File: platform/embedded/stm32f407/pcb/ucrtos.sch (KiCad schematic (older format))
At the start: 7 parts, among them J1 nes_gamepad, J2 STM32F4_Discovery_Header

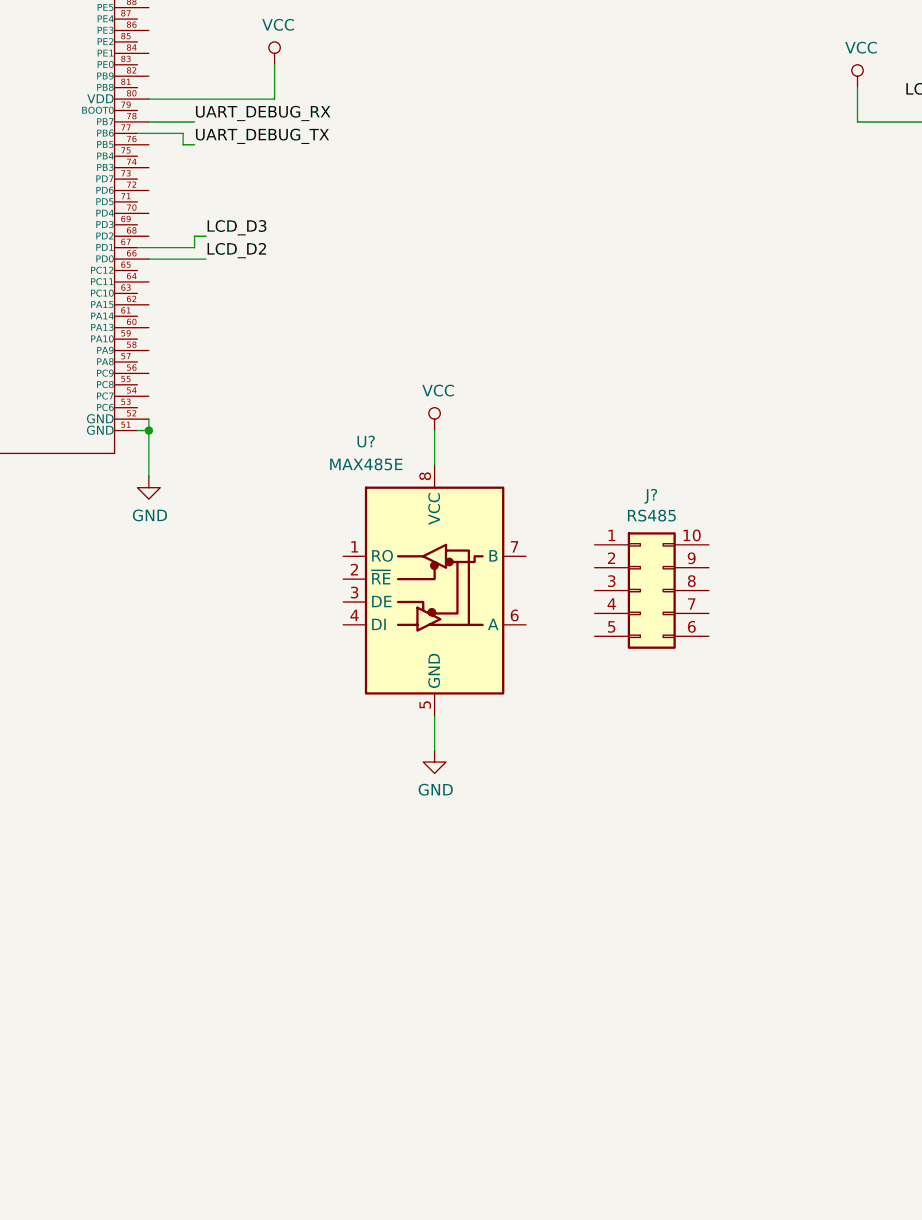
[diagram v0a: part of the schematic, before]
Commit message: platform stm32f4: pcb: add NRF24
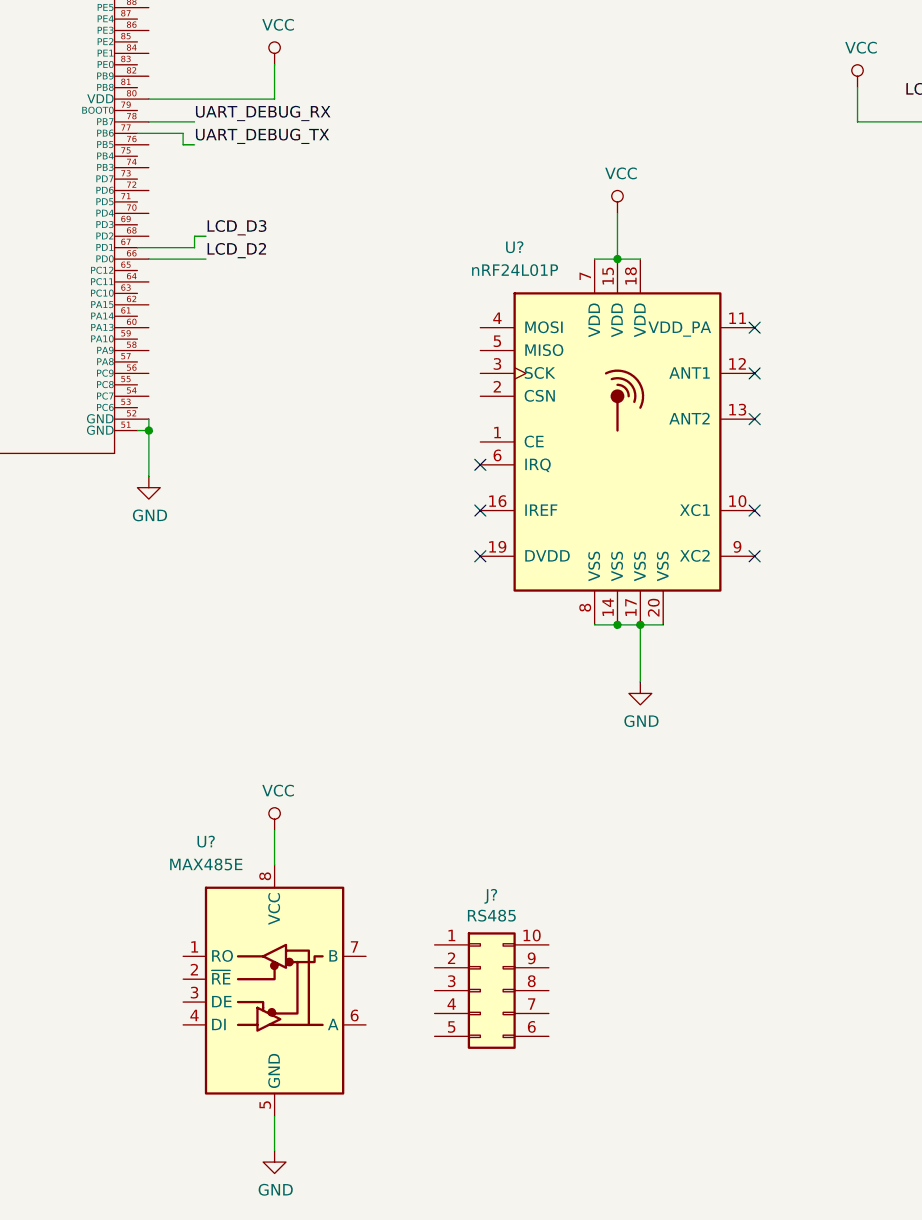
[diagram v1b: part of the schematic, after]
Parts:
- added U?: nRF24L01P, Package_DFN_QFN:QFN-20-1EP_4x4mm_P0.5mm_EP2.5x2.5mm, symbol RF:nRF24L01P
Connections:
- net GND: now also U?.14 (VSS), U?.17 (VSS), U?.20 (VSS), U?.8 (VSS)
- net VCC: now also U?.15 (VDD), U?.18 (VDD), U?.7 (VDD)
- no-connect marks 13 -> 21
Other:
- moved on the sheet: J?, U?
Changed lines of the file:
@@
 L Interface_UART:MAX485E U?
 U 1 1 5C438854
-P 6150 4450
-F 0 "U?" H 5850 5050 50  0000 C CNN
-F 1 "MAX485E" H 5850 4950 50  0000 C CNN
-F 2 "" H 6150 3750 50  0001 C CNN
-F 3 "https://datasheets.maximintegrated.com/en/ds/MAX1487E-MAX491E.pdf" H 6150 4500 50  0001 C CNN
-	1    6150 4450
+P 5450 6200
+F 0 "U?" H 5150 6800 50  0000 C CNN
+F 1 "MAX485E" H 5150 6700 50  0000 C CNN
+F 2 "" H 5450 5500 50  0001 C CNN
+F 3 "https://datasheets.maximintegrated.com/en/ds/MAX1487E-MAX491E.pdf" H 5450 6250 50  0001 C CNN
+	1    5450 6200
 	1    0    0    -1
 $EndComp
@@
 L Connector_Generic:Conn_02x05_Counter_Clockwise J?
 U 1 1 5C438977
-P 7050 4500
-F 0 "J?" H 7100 4917 50  0000 C CNN
-F 1 "RS485" H 7100 4826 50  0000 C CNN
-F 2 "" H 7050 4500 50  0001 C CNN
-F 3 "~" H 7050 4500 50  0001 C CNN
-	1    7050 4500
+P 6350 6250
+F 0 "J?" H 6400 6667 50  0000 C CNN
+F 1 "RS485" H 6400 6576 50  0000 C CNN
+F 2 "" H 6350 6250 50  0001 C CNN
+F 3 "~" H 6350 6250 50  0001 C CNN
+	1    6350 6250
 	1    0    0    -1
 $EndComp
@@
 L power:VCC #PWR?
 U 1 1 5C4EA333
-P 6150 3800
-F 0 "#PWR?" H 6150 3650 50  0001 C CNN
-F 1 "VCC" H 6167 3973 50  0000 C CNN
-F 2 "" H 6150 3800 50  0001 C CNN
-F 3 "" H 6150 3800 50  0001 C CNN
-	1    6150 3800
-	1    0    0    -1
-$EndComp
-Wire Wire Line
-	6150 3800 6150 3950
+P 5450 5550
+F 0 "#PWR?" H 5450 5400 50  0001 C CNN
+F 1 "VCC" H 5467 5723 50  0000 C CNN
+F 2 "" H 5450 5550 50  0001 C CNN
+F 3 "" H 5450 5550 50  0001 C CNN
+	1    5450 5550
+	1    0    0    -1
+$EndComp
+Wire Wire Line
+	5450 5550 5450 5700
 $Comp
 L power:GND #PWR?
 U 1 1 5C4EB213
-P 6150 5200
-F 0 "#PWR?" H 6150 4950 50  0001 C CNN
-F 1 "GND" H 6155 5027 50  0000 C CNN
-F 2 "" H 6150 5200 50  0001 C CNN
-F 3 "" H 6150 5200 50  0001 C CNN
-	1    6150 5200
-	1    0    0    -1
-$EndComp
-Wire Wire Line
-	6150 5050 6150 5200
+P 5450 6950
+F 0 "#PWR?" H 5450 6700 50  0001 C CNN
+F 1 "GND" H 5455 6777 50  0000 C CNN
+F 2 "" H 5450 6950 50  0001 C CNN
+F 3 "" H 5450 6950 50  0001 C CNN
+	1    5450 6950
+	1    0    0    -1
+$EndComp
+Wire Wire Line
+	5450 6800 5450 6950
 $Comp
 L power:VCC #PWR?
@@
 Text Label 5100 2450 0    50   ~ 0
 UART_DEBUG_RX
+$Comp
+L RF:nRF24L01P U?
+U 1 1 5C63E83C
+P 6950 3850
+F 0 "U?" H 6500 4700 50  0000 C CNN
+F 1 "nRF24L01P" H 6500 4600 50  0000 C CNN
+F 2 "Package_DFN_QFN:QFN-20-1EP_4x4mm_P0.5mm_EP2.5x2.5mm" H 7150 4650 50  0001 L CIN
+F 3 "http://www.nordicsemi.com/eng/content/download/2726/34069/file/nRF24L01P_Product_Specification_1_0.pdf" H 6950 3950 50  0001 C CNN
+	1    6950 3850
+	1    0    0    -1
+$EndComp
+NoConn ~ 7550 3550
+NoConn ~ 7550 3750
+NoConn ~ 7550 4150
+NoConn ~ 7550 4350
+$Comp
+L power:GND #PWR?
+U 1 1 5C657D22
+P 7050 4900
+F 0 "#PWR?" H 7050 4650 50  0001 C CNN
+F 1 "GND" H 7055 4727 50  0000 C CNN
+F 2 "" H 7050 4900 50  0001 C CNN
+F 3 "" H 7050 4900 50  0001 C CNN
+	1    7050 4900
+	1    0    0    -1
+$EndComp
+Wire Wire Line
+	6850 4650 6950 4650
+Connection ~ 6950 4650
+Wire Wire Line
+	6950 4650 7050 4650
+Connection ~ 7050 4650
+Wire Wire Line
+	7050 4650 7150 4650
+$Comp
+L power:VCC #PWR?
+U 1 1 5C662322
+P 6950 2850
+F 0 "#PWR?" H 6950 2700 50  0001 C CNN
+F 1 "VCC" H 6967 3023 50  0000 C CNN
+F 2 "" H 6950 2850 50  0001 C CNN
+F 3 "" H 6950 2850 50  0001 C CNN
+	1    6950 2850
+	1    0    0    -1
+$EndComp
+Wire Wire Line
+	6850 3050 6950 3050
+Connection ~ 6950 3050
+Wire Wire Line
+	6950 3050 7050 3050
+Wire Wire Line
+	6950 3050 6950 2850
+Wire Wire Line
+	7050 4650 7050 4900
+NoConn ~ 6350 3950
+NoConn ~ 6350 4150
+NoConn ~ 6350 4350
+NoConn ~ 7550 3350
 $EndSCHEMATC

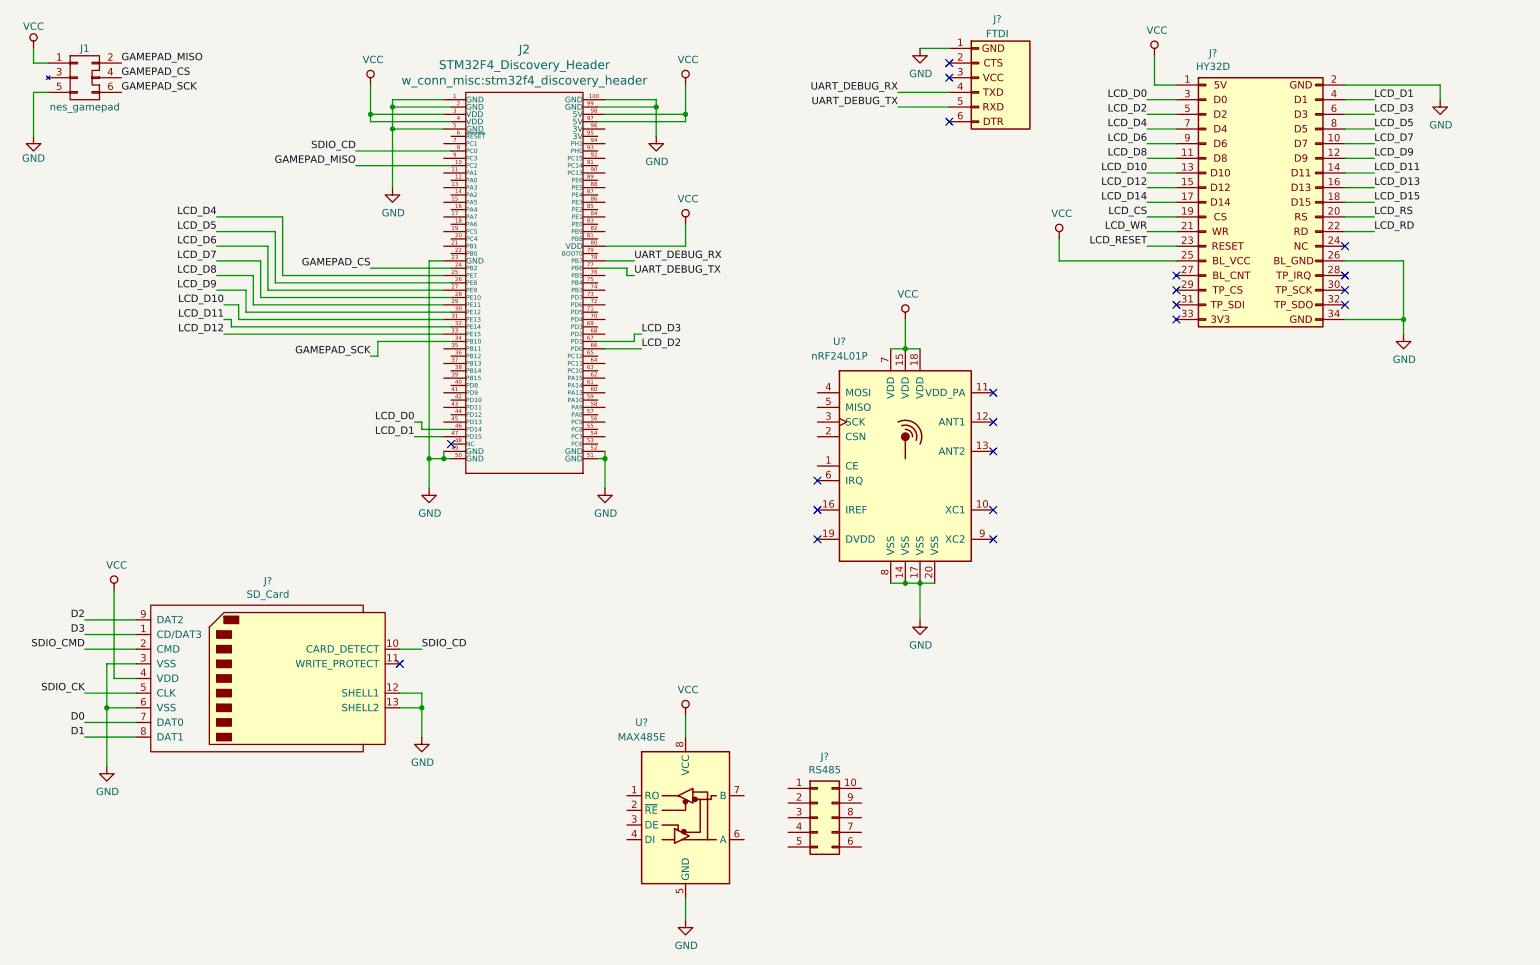
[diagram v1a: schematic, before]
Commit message: platform stm32f4: pcb: wire NRF24
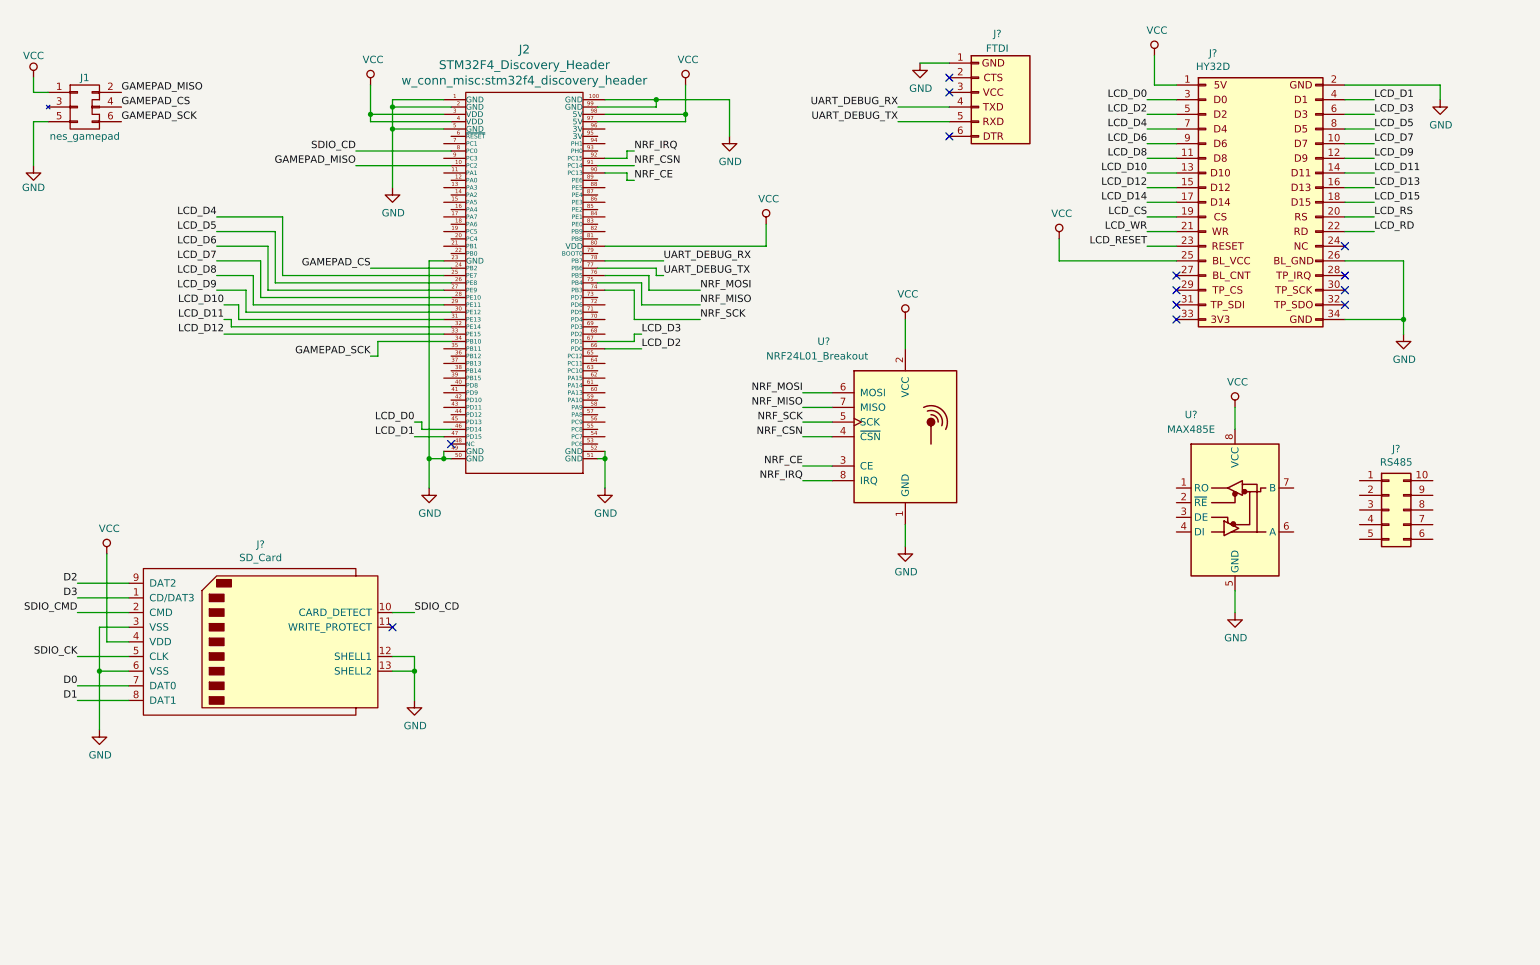
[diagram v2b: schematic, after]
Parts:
- removed U?: nRF24L01P, Package_DFN_QFN:QFN-20-1EP_4x4mm_P0.5mm_EP2.5x2.5mm, symbol RF:nRF24L01P
- added U?: NRF24L01_Breakout, RF_Module:nRF24L01_Breakout, symbol RF:NRF24L01_Breakout
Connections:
- net GND: now also U?.1 (GND)
- net VCC: now also U?.2 (VCC)
- net NRF_SCK: now reaches J2.74 (PB3)
- net NRF_SCK: now also U?.5 (SCK)
- net NRF_MISO: now reaches J2.75 (PB4)
- net NRF_MISO: now also U?.7 (MISO)
- net NRF_MOSI: now reaches J2.76 (PB5)
- net NRF_MOSI: now also U?.6 (MOSI)
- net NRF_CE: now reaches J2.90 (PC13)
- net NRF_CE: now also U?.3 (CE)
- net NRF_CSN: now reaches J2.91 (PC14)
- net NRF_CSN: now also U?.4 (~CSN)
- net NRF_IRQ: now reaches J2.92 (PC15)
- net NRF_IRQ: now also U?.8 (IRQ)
- no-connect marks 21 -> 13
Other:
- moved on the sheet: J1, J?, U?

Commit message: platform stm32f4: pcb: update schematics
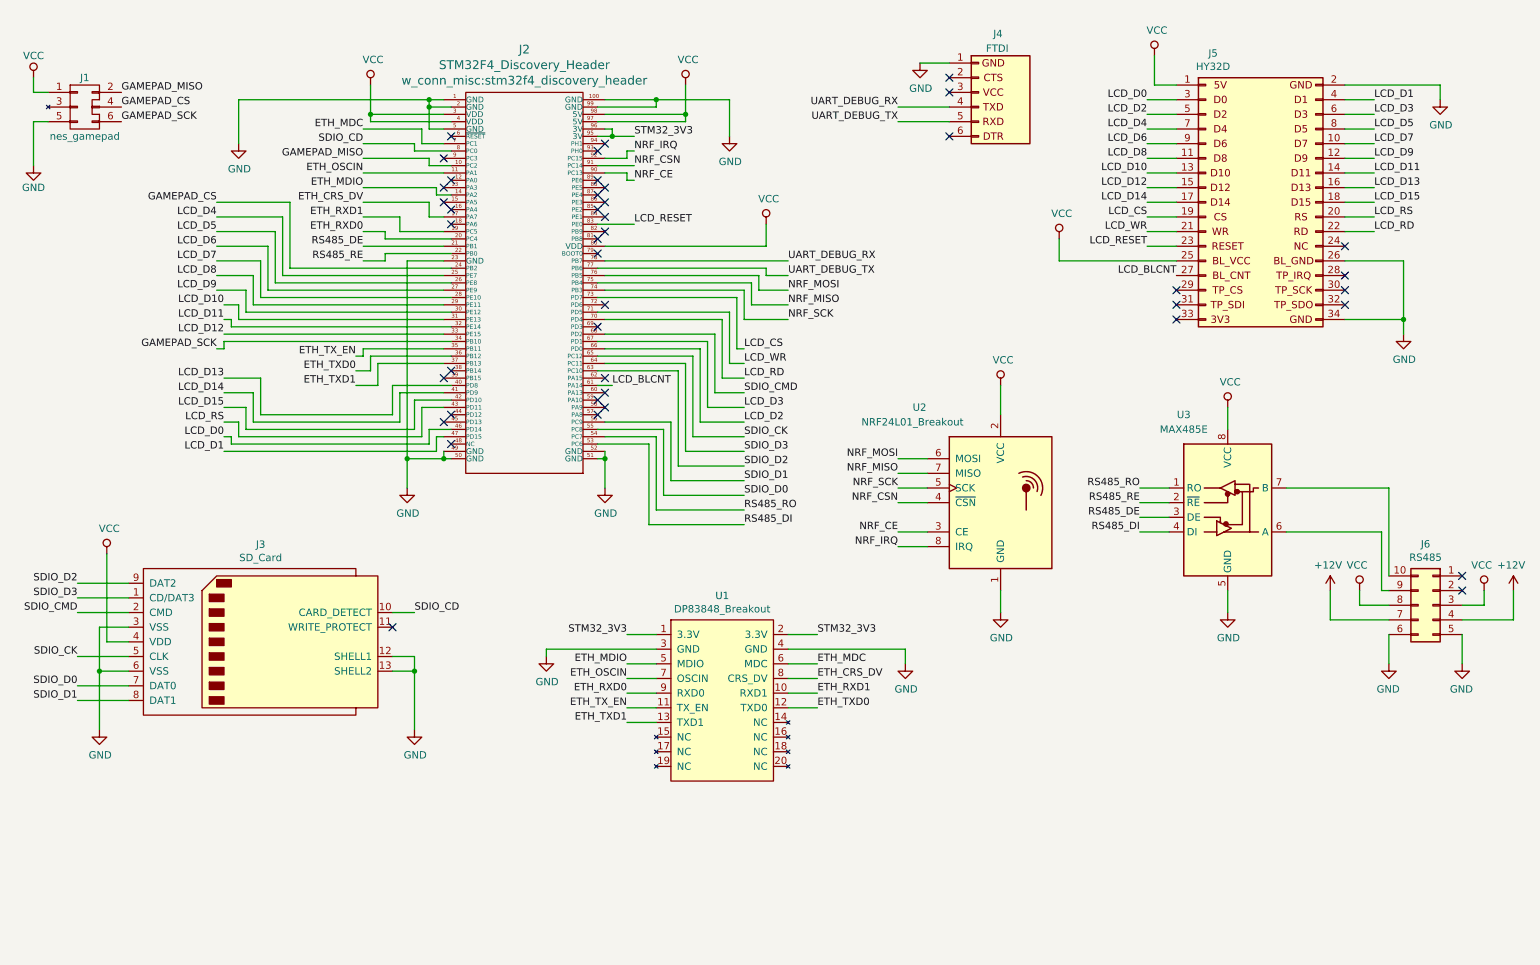
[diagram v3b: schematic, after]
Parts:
- added U1: DP83848_Breakout, symbol dp83848:DP83848_Breakout
- gave numbers to parts that had none: 6
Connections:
- net D0 is gone; now on net SDIO_D0: J3.7 (DAT0)
- net D1 is gone; now on net SDIO_D1: J3.8 (DAT1)
- net D2 is gone; now on net SDIO_D2: J3.9 (DAT2)
- net D3 is gone; now on net SDIO_D3: J3.1 (CD/DAT3)
- net GND: now also J6.5 (Pin_5), J6.6 (Pin_6), U1.3 (GND), U1.4 (GND)
- net LCD_CS: now also J2.73 (PD7)
- net LCD_D13: now also J2.40 (PD8)
- net LCD_D14: now also J2.41 (PD9)
- net LCD_D15: now also J2.42 (PD10)
- net LCD_RD: now also J2.70 (PD4)
- net LCD_RESET: now also J2.83 (PE0)
- net LCD_RS: now also J2.43 (PD11)
- net LCD_WR: now also J2.71 (PD5)
- net SDIO_CK: now also J2.65 (PC12)
- net SDIO_CMD: now also J2.68 (PD2)
- net VCC: now also J6.3 (Pin_3), J6.8 (Pin_8)
- net ETH_OSCIN: now reaches J2.11 (PA1)
- net ETH_OSCIN: now also U1.7 (OSCIN)
- net ETH_MDIO: now reaches J2.14 (PA2)
- net ETH_MDIO: now also U1.5 (MDIO)
- net ETH_CRS_DV: now reaches J2.17 (PA7)
- net ETH_CRS_DV: now also U1.8 (CRS_DV)
- net ETH_RXD1: now reaches J2.19 (PC5)
- net ETH_RXD1: now also U1.10 (RXD1)
- net ETH_RXD0: now reaches J2.20 (PC4)
- net ETH_RXD0: now also U1.9 (RXD0)
- net RS485_DE: now reaches J2.21 (PB1)
- net RS485_DE: now also U3.3 (DE)
- net RS485_RE: now reaches J2.22 (PB0)
- net RS485_RE: now also U3.2 (~RE)
- net ETH_TX_EN: now reaches J2.35 (PB11)
- net ETH_TX_EN: now also U1.11 (TX_EN)
- net ETH_TXD0: now reaches J2.36 (PB12)
- net ETH_TXD0: now also U1.12 (TXD0)
- net ETH_TXD1: now reaches J2.37 (PB13)
- net ETH_TXD1: now also U1.13 (TXD1)
- net RS485_DI: now reaches J2.53 (PC6)
- net RS485_DI: now also U3.4 (DI)
- net RS485_RO: now reaches J2.54 (PC7)
- net RS485_RO: now also U3.1 (RO)
- net SDIO_D0: now reaches J2.55 (PC8)
- net SDIO_D1: now reaches J2.56 (PC9)
- net LCD_BLCNT: now reaches J2.61 (PA14)
- net LCD_BLCNT: now also J5.27 (D13)
- net SDIO_D2: now reaches J2.63 (PC10)
- net SDIO_D3: now reaches J2.64 (PC11)
- net ETH_MDC: now reaches J2.7 (PC1)
- net ETH_MDC: now also U1.6 (MDC)
- net STM32_3V3: now reaches J2.95 (3V)
- net STM32_3V3: now also J2.96 (3V), U1.1 (3.3V), U1.2 (3.3V)
- net at U3.6 (A): now also J6.9 (Pin_9)
- net at U3.7 (B): now also J6.10 (Pin_10)
- net +12V: now reaches J6.4 (Pin_4)
- net +12V: now also J6.7 (Pin_7)
- no-connect marks 13 -> 43
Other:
- moved on the sheet: J6, U2, U3
